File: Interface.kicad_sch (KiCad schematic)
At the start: 22 parts, among them J10 I2C, J11 Keyboard 1, J12 Keyboard 2, J13 Keyboard 2, J4 Keyboard 1, J5 UART, J6 RS485, J7 Extra, J8 USB_A, J9 CAN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

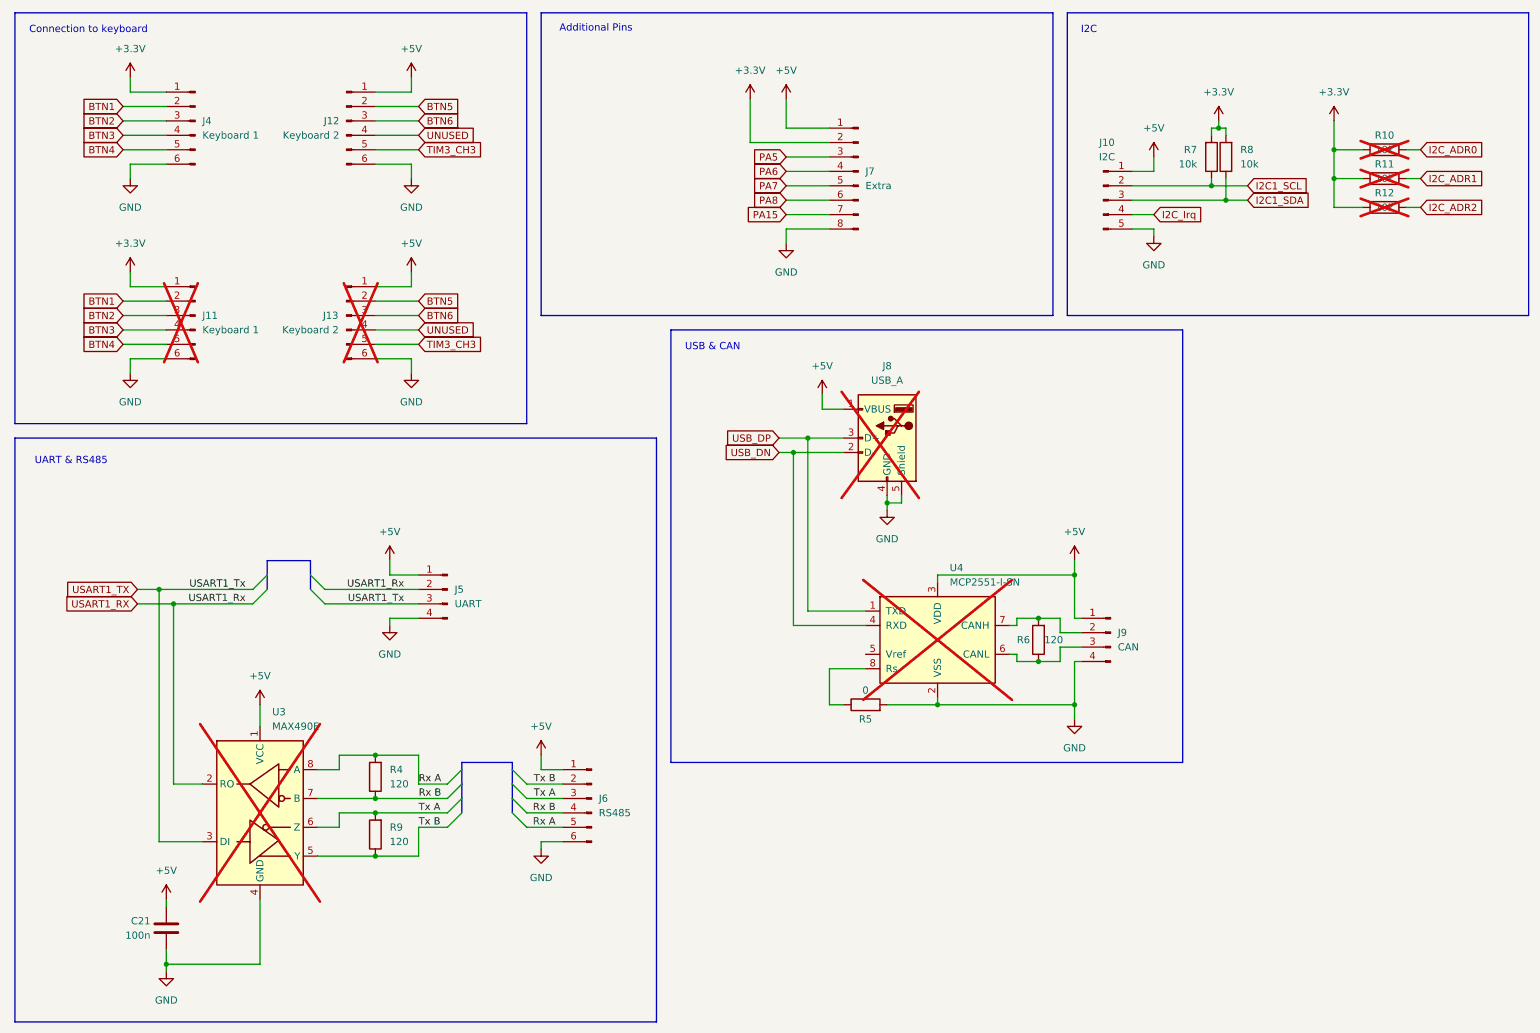
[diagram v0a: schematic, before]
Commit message: - Created head board tilable up to 4x - Placed and routed lines ToDo: - Print - I2C reanbable
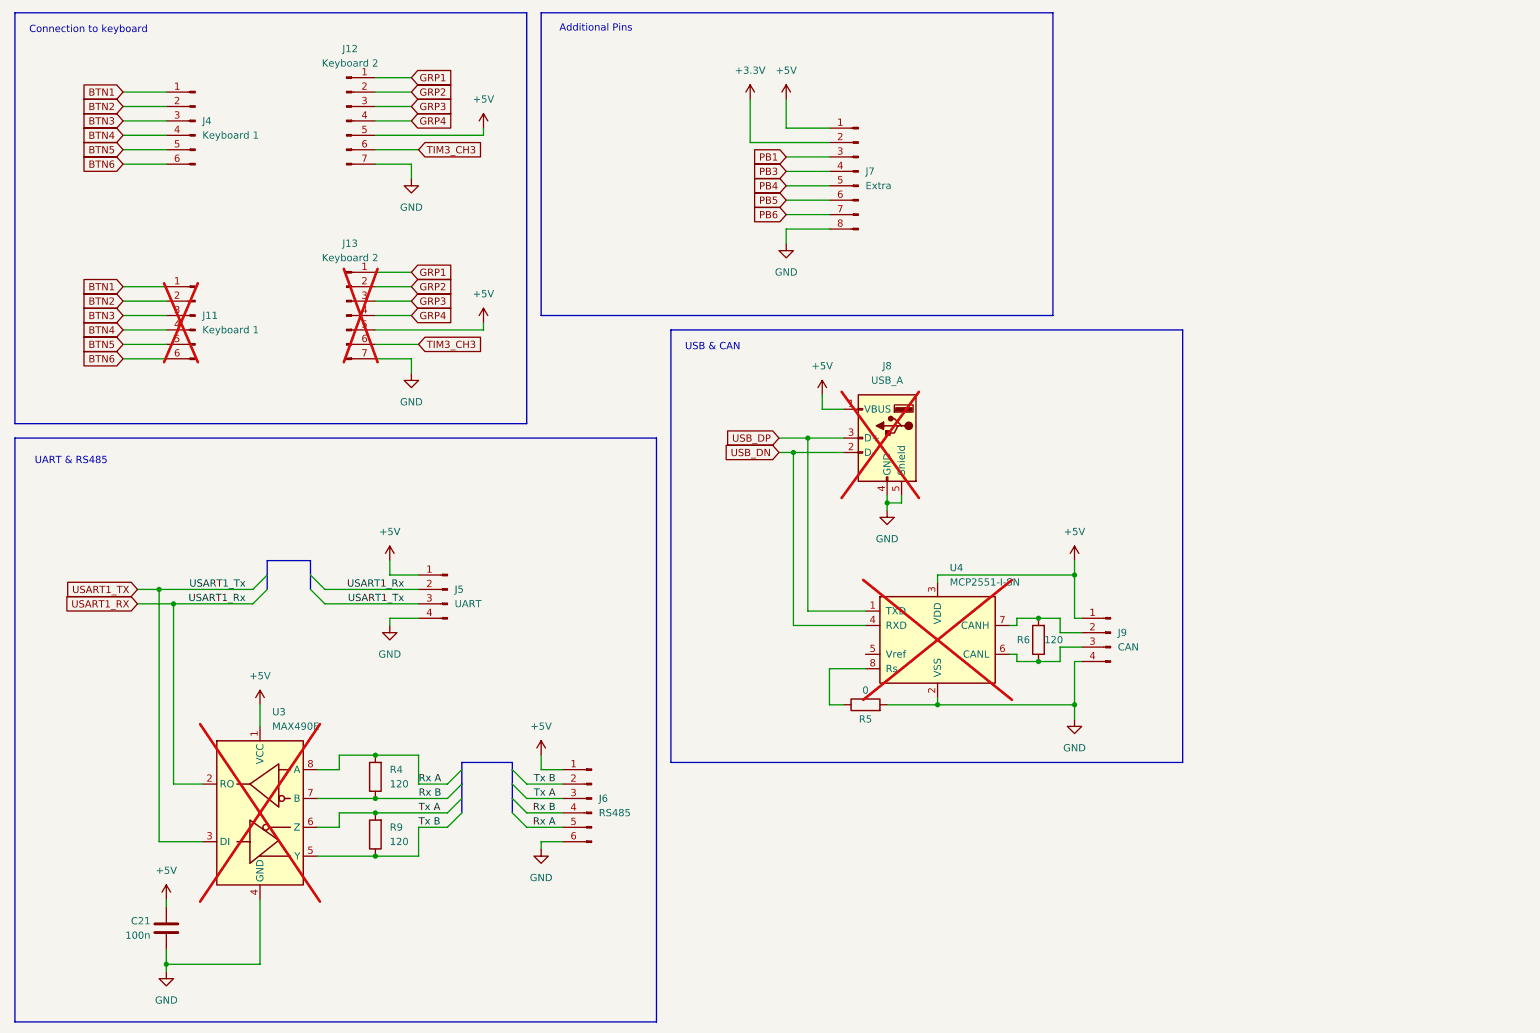
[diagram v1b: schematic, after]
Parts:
- removed J10: I2C, Library:Conn_Edge_x05, symbol Connector:Conn_01x05_Pin
- removed J13: Keyboard 2, Connector_PinHeader_2.54mm:PinHeader_1x06_P2.54mm_Vertical, symbol Connector:Conn_01x06_Pin
- removed R10, R11, R12, R7, R8: 10k, Resistor_SMD:R_0805_2012Metric_Pad1.20x1.40mm_HandSolder, symbol Device:R
- added J13: Keyboard 2, Connector_PinHeader_2.54mm:PinHeader_1x07_P2.54mm_Vertical, symbol Connector:Conn_01x07_Pin
- J12: footprint Connector_PinHeader_2.54mm:PinHeader_1x06_P2.54mm_Vertical_SMD_Pin1Left -> Connector_PinHeader_2.54mm:PinHeader_1x07_P2.54mm_Vertical_SMD_Pin1Left; symbol Connector:Conn_01x06_Pin -> Connector:Conn_01x07_Pin
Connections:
- net +3.3V: no longer J11.1 (Pin_1), J4.1 (Pin_1)
- net +5V: now also J12.5 (Pin_5), J13.5 (Pin_5); no longer J12.1 (Pin_1)
- net BTN1: now also J11.1 (Pin_1), J4.1 (Pin_1); no longer J11.2 (Pin_2), J4.2 (Pin_2)
- net BTN2: now also J11.2 (Pin_2), J4.2 (Pin_2); no longer J11.3 (Pin_3), J4.3 (Pin_3)
- net BTN3: now also J11.3 (Pin_3), J4.3 (Pin_3); no longer J11.4 (Pin_4), J4.4 (Pin_4)
- net BTN4: now also J11.4 (Pin_4), J4.4 (Pin_4); no longer J11.5 (Pin_5), J4.5 (Pin_5)
- net BTN5: now also J11.5 (Pin_5), J4.5 (Pin_5); no longer J12.2 (Pin_2)
- net BTN6: now also J11.6 (Pin_6), J4.6 (Pin_6); no longer J12.3 (Pin_3)
- net GND: now also J12.7 (Pin_7), J13.7 (Pin_7); no longer J11.6 (Pin_6), J12.6 (Pin_6), J4.6 (Pin_6)
- net TIM3_CH3: now also J12.6 (Pin_6), J13.6 (Pin_6); no longer J12.5 (Pin_5)
- net PA15 renamed PB6
- net PA5 renamed PB1
- net PA6 renamed PB3
- net PA7 renamed PB4
- net PA8 renamed PB5
- net UNUSED renamed GRP4
- net GRP4: now also J13.4 (Pin_4)
- new net GRP1: J12.1 (Pin_1), J13.1 (Pin_1)
- new net GRP2: J12.2 (Pin_2), J13.2 (Pin_2)
- new net GRP3: J12.3 (Pin_3), J13.3 (Pin_3)
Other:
- note removed: "I2C"

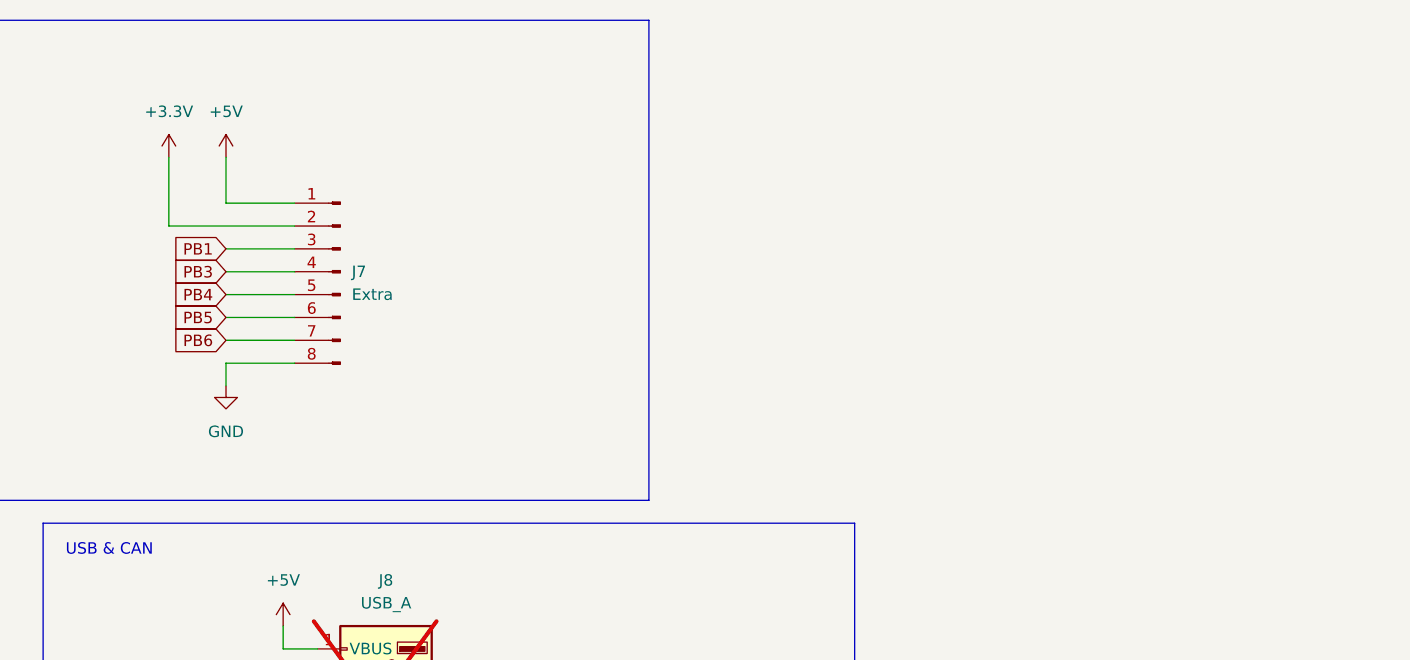
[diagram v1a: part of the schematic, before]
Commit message: - Added Pull Ups for I2C - Added second reset button on bottom side
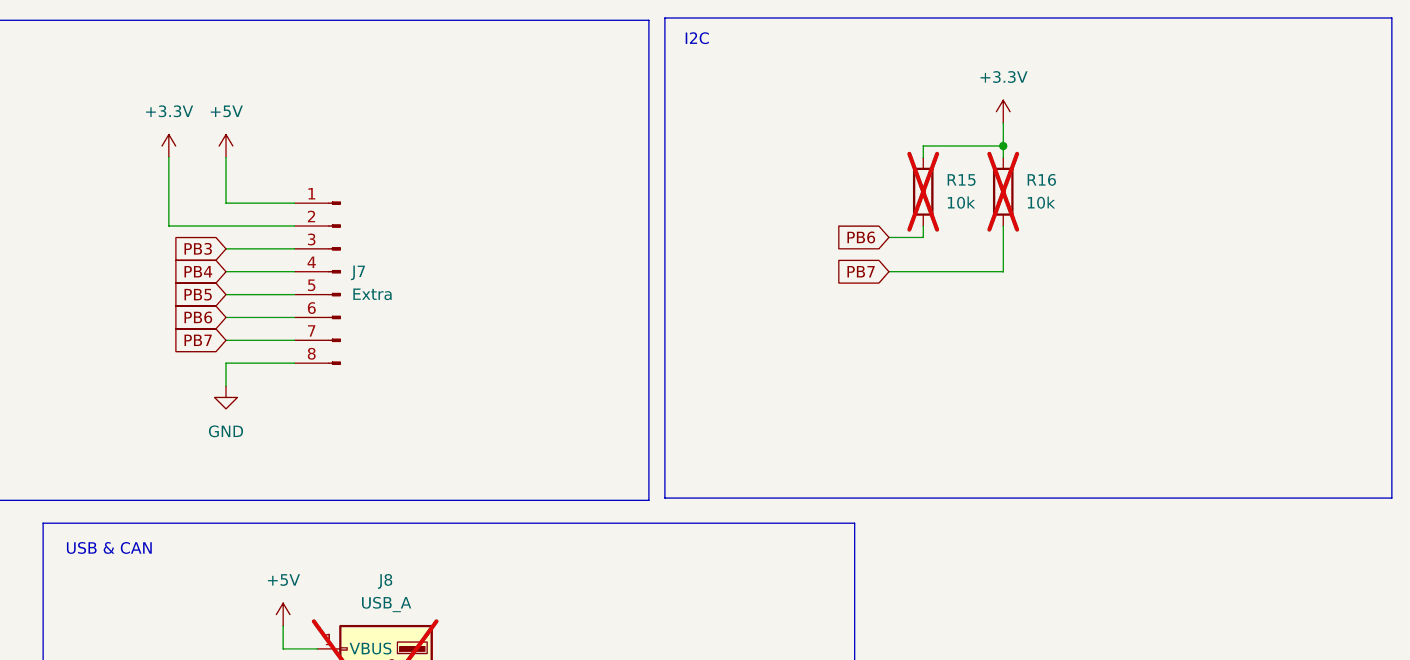
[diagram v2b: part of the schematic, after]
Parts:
- added R15, R16: 10k, Resistor_SMD:R_0805_2012Metric_Pad1.20x1.40mm_HandSolder, symbol Device:R
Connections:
- net PB1 is gone; now on net PB3: J7.3 (Pin_3)
- net +3.3V: now also R15.2, R16.2
- net PB3: no longer J7.4 (Pin_4)
- net PB4: now also J7.4 (Pin_4); no longer J7.5 (Pin_5)
- net PB5: now also J7.5 (Pin_5); no longer J7.6 (Pin_6)
- net PB6: now also J7.6 (Pin_6), R15.1; no longer J7.7 (Pin_7)
- new net PB7: J7.7 (Pin_7), R16.1
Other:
- note added: "I2C"

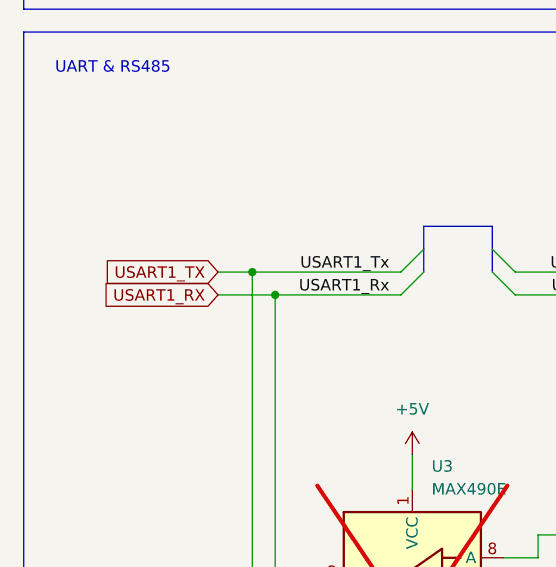
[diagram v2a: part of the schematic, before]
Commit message: - Added missing library files to git - Added logo to silkscreen - ERC: Okay
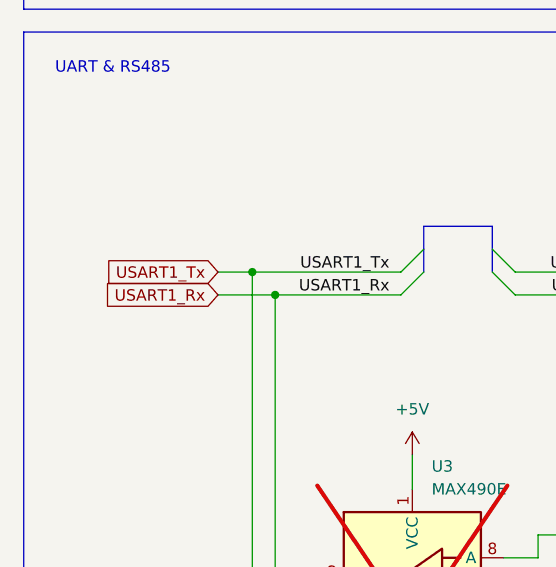
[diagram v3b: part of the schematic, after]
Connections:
- net USART1_RX renamed USART1_Rx
- net USART1_TX renamed USART1_Tx
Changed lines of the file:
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@@
 		)
 	)
-	(global_label "USART1_TX"
+	(global_label "USART1_Tx"
 		(shape input)
 		(at 38.1 118.11 180)
@@
 		)
 	)
-	(global_label "USART1_RX"
+	(global_label "USART1_Rx"
 		(shape input)
 		(at 38.1 120.65 180)
